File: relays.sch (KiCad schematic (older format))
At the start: 4 parts, among them U2 MCP23017-E_SP

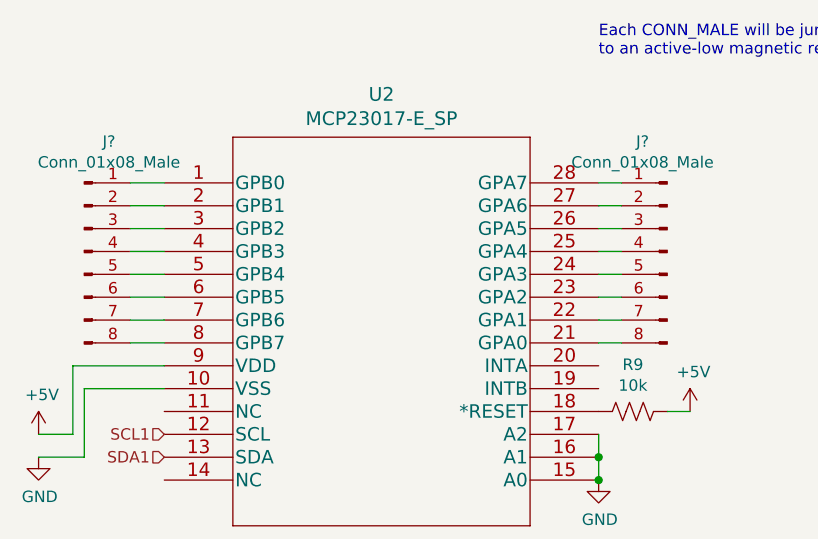
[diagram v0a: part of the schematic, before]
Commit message: Got rid of overlying duplicate parts
Some identical parts were placed over eachother which showed up when annotating references
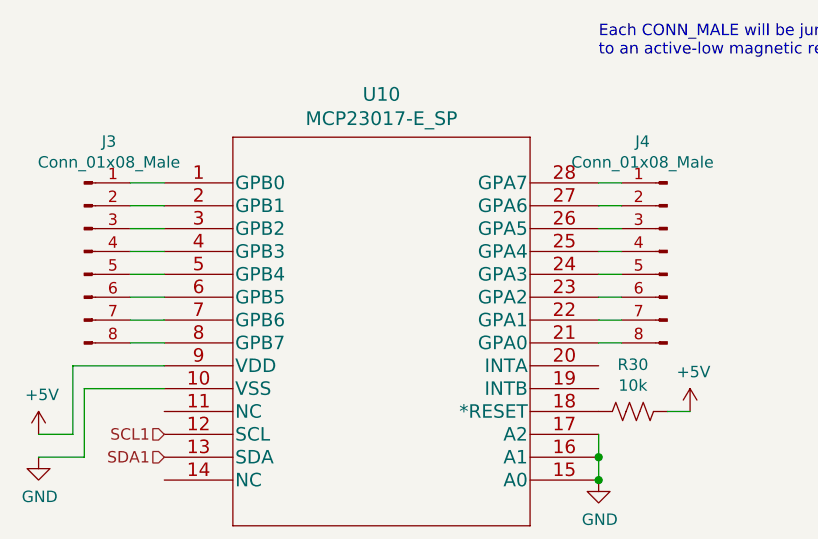
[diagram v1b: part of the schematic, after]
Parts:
- gave numbers to parts that had none: 2
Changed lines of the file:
@@
 SCL1
-$Comp
-L 2020-09-01_02-26-45:MCP23017-E_SP U2
-U 1 1 5F5A3B8E
-P 5000 2200
-AR Path="/5F57B52C/5F5A3B8E" Ref="U2"  Part="1"
-AR Path="/5F7C211E/5F5A3B8E" Ref="U?"  Part="1"
-F 0 "U?" H 5950 2587 60  0000 C CNN
-F 1 "MCP23017-E_SP" H 5950 2481 60  0000 C CNN
-F 2 "SPDIP28_300MC_MCH" H 5950 2440 60  0001 C CNN
-F 3 "" H 5000 2200 60  0000 C CNN
-	1    5000 2200
-	1    0    0    -1
-$EndComp
-Wire Wire Line
-	6900 3500 6900 3400
-Connection ~ 6900 3400
-Wire Wire Line
-	6900 3400 6900 3300
 $Comp
 L Device:R_US R9
@@
 P 7050 3200
 AR Path="/5F57B52C/5F5A3B84" Ref="R9"  Part="1"
-AR Path="/5F7C211E/5F5A3B84" Ref="R?"  Part="1"
-F 0 "R?" V 6845 3200 50  0000 C CNN
+AR Path="/5F7C211E/5F5A3B84" Ref="R30"  Part="1"
+F 0 "R30" V 6845 3200 50  0000 C CNN
 F 1 "10k" V 6936 3200 50  0000 C CNN
 F 2 "" V 7090 3190 50  0001 C CNN
@@
 $Comp
 L power:+5V #PWR0101
-U 1 1 5F5A3B7D
+U 1 1 5F733068
 P 7300 3200
-AR Path="/5F57B52C/5F5A3B7D" Ref="#PWR0101"  Part="1"
-AR Path="/5F7C211E/5F5A3B7D" Ref="#PWR?"  Part="1"
-F 0 "#PWR?" H 7300 3050 50  0001 C CNN
+AR Path="/5F57B52C/5F733068" Ref="#PWR0101"  Part="1"
+AR Path="/5F7C211E/5F733068" Ref="#PWR0153"  Part="1"
+F 0 "#PWR0153" H 7300 3050 50  0001 C CNN
 F 1 "+5V" H 7315 3373 50  0000 C CNN
 F 2 "" H 7300 3200 50  0001 C CNN
@@
 	1    0    0    -1
 $EndComp
-Connection ~ 6900 3500
 $Comp
 L power:GND #PWR0102
-U 1 1 5F5A3B69
+U 1 1 5F733065
 P 6900 3500
-AR Path="/5F57B52C/5F5A3B69" Ref="#PWR0102"  Part="1"
-AR Path="/5F7C211E/5F5A3B69" Ref="#PWR?"  Part="1"
-F 0 "#PWR?" H 6900 3250 50  0001 C CNN
+AR Path="/5F57B52C/5F733065" Ref="#PWR0102"  Part="1"
+AR Path="/5F7C211E/5F733065" Ref="#PWR0154"  Part="1"
+F 0 "#PWR0154" H 6900 3250 50  0001 C CNN
 F 1 "GND" H 6905 3327 50  0000 C CNN
 F 2 "" H 6900 3500 50  0001 C CNN
@@
 $Comp
 L power:GND #PWR0103
-U 1 1 5F5A3B6F
+U 1 1 5F733066
 P 4450 3400
-AR Path="/5F57B52C/5F5A3B6F" Ref="#PWR0103"  Part="1"
-AR Path="/5F7C211E/5F5A3B6F" Ref="#PWR?"  Part="1"
-F 0 "#PWR?" H 4450 3150 50  0001 C CNN
+AR Path="/5F57B52C/5F733066" Ref="#PWR0103"  Part="1"
+AR Path="/5F7C211E/5F733066" Ref="#PWR0155"  Part="1"
+F 0 "#PWR0155" H 4450 3150 50  0001 C CNN
 F 1 "GND" H 4455 3227 50  0000 C CNN
 F 2 "" H 4450 3400 50  0001 C CNN
@@
 $Comp
 L power:+5V #PWR0104
-U 1 1 5F5A3B75
+U 1 1 5F733067
 P 4450 3300
-AR Path="/5F57B52C/5F5A3B75" Ref="#PWR0104"  Part="1"
-AR Path="/5F7C211E/5F5A3B75" Ref="#PWR?"  Part="1"
-F 0 "#PWR?" H 4450 3150 50  0001 C CNN
+AR Path="/5F57B52C/5F733067" Ref="#PWR0104"  Part="1"
+AR Path="/5F7C211E/5F733067" Ref="#PWR0156"  Part="1"
+F 0 "#PWR0156" H 4450 3150 50  0001 C CNN
 F 1 "+5V" H 4465 3473 50  0000 C CNN
 F 2 "" H 4450 3300 50  0001 C CNN
@@
 	4650 3400 4450 3400
 $Comp
-L Connector:Conn_01x08_Male J?
+L Connector:Conn_01x08_Male J3
 U 1 1 5F7D661D
 P 4650 2500
-F 0 "J?" H 4758 2981 50  0000 C CNN
+F 0 "J3" H 4758 2981 50  0000 C CNN
 F 1 "Conn_01x08_Male" H 4758 2890 50  0000 C CNN
 F 2 "" H 4650 2500 50  0001 C CNN
@@
 $EndComp
 $Comp
-L Connector:Conn_01x08_Male J?
+L Connector:Conn_01x08_Male J4
 U 1 1 5F7DB213
 P 7200 2500
-F 0 "J?" H 7308 2981 50  0000 C CNN
+F 0 "J4" H 7308 2981 50  0000 C CNN
 F 1 "Conn_01x08_Male" H 7308 2890 50  0000 C CNN
 F 2 "" H 7200 2500 50  0001 C CNN
@@
 Text Notes 6900 1650 0    50   ~ 0
 Each CONN_MALE will be jumped\nto an active-low magnetic relay
+Wire Wire Line
+	6900 3400 6900 3300
+Wire Wire Line
+	6900 3500 6900 3400
+Connection ~ 6900 3400
+Connection ~ 6900 3500
+$Comp
+L 2020-09-01_02-26-45:MCP23017-E_SP U2
+U 1 1 5F73306A
+P 5000 2200
+AR Path="/5F57B52C/5F73306A" Ref="U2"  Part="1"
+AR Path="/5F7C211E/5F73306A" Ref="U10"  Part="1"
+F 0 "U10" H 5950 2587 60  0000 C CNN
+F 1 "MCP23017-E_SP" H 5950 2481 60  0000 C CNN
+F 2 "SPDIP28_300MC_MCH" H 5950 2440 60  0001 C CNN
+F 3 "" H 5000 2200 60  0000 C CNN
+	1    5000 2200
+	1    0    0    -1
+$EndComp
 $EndSCHEMATC

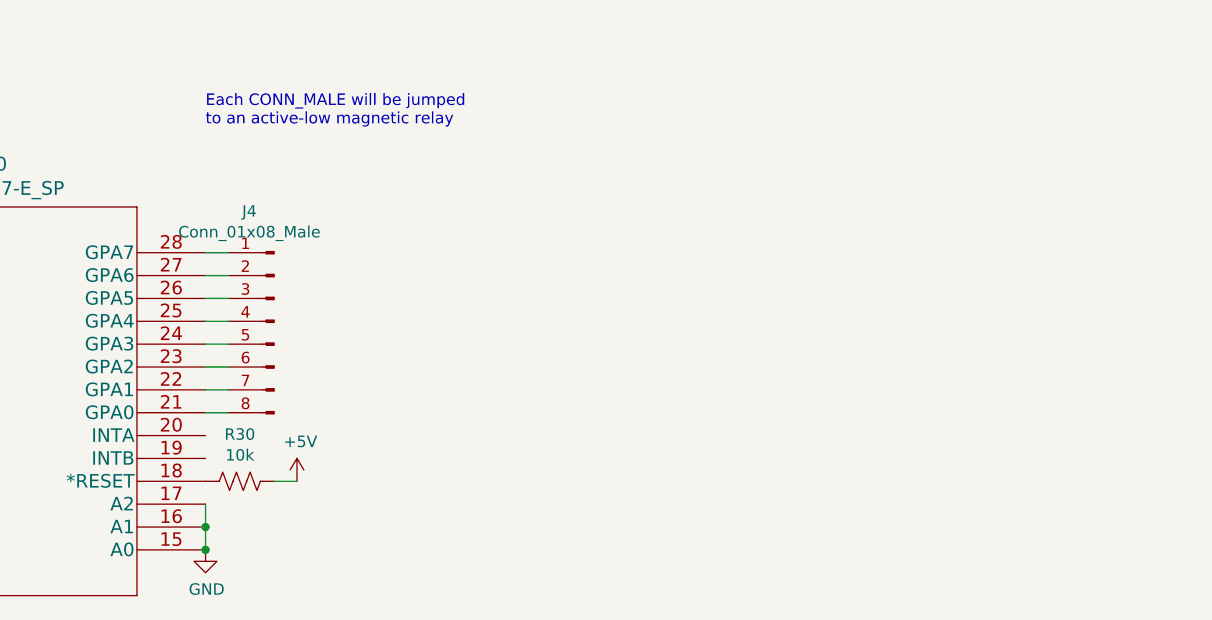
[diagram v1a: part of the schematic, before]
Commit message: Added Relays and diodes
Added relays and diodes per reviewer suggestion on the remote side connected to the MCP23017.
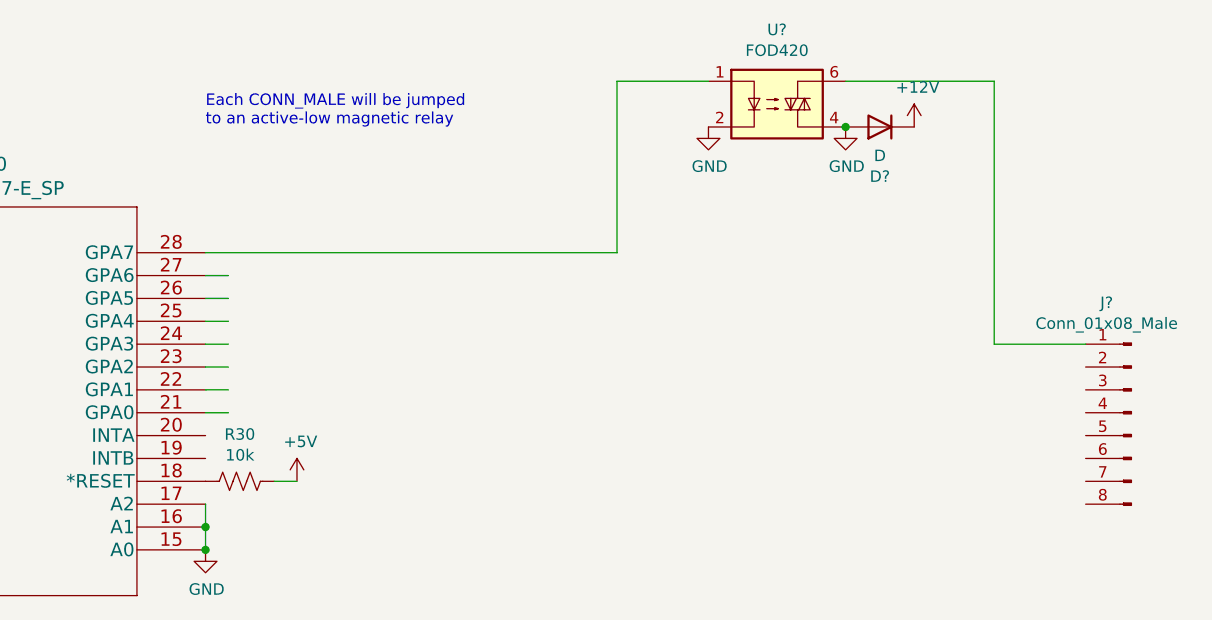
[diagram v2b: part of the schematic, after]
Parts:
- removed J4: Conn_01x08_Male, symbol Connector:Conn_01x08_Male
- added D?: D, symbol Device:D
- added J?: Conn_01x08_Male, symbol Connector:Conn_01x08_Male
- added U?: FOD420, Package_DIP:DIP-6_W7.62mm, symbol Relay_SolidState:FOD420
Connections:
- net labels added: +12V
- wire segments 25 -> 30
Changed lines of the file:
@@
 	1    0    0    -1
-$EndComp
-$Comp
-L Connector:Conn_01x08_Male J4
-U 1 1 5F7DB213
-P 7200 2500
-F 0 "J4" H 7308 2981 50  0000 C CNN
-F 1 "Conn_01x08_Male" H 7308 2890 50  0000 C CNN
-F 2 "" H 7200 2500 50  0001 C CNN
-F 3 "~" H 7200 2500 50  0001 C CNN
-	1    7200 2500
-	-1   0    0    -1
 $EndComp
 Wire Wire Line
@@
 	4850 2900 5000 2900
 Wire Wire Line
-	6900 2200 7000 2200
-Wire Wire Line
 	7000 2300 6900 2300
 Wire Wire Line
@@
 Wire Wire Line
 	7000 2900 6900 2900
-Text Notes 6900 1650 0    50   ~ 0
-Each CONN_MALE will be jumped\nto an active-low magnetic relay
 Wire Wire Line
 	6900 3400 6900 3300
@@
 	1    0    0    -1
 $EndComp
+Text Notes 6900 1650 0    50   ~ 0
+Each CONN_MALE will be jumped\nto an active-low magnetic relay
+$Comp
+L Relay_SolidState:FOD420 U?
+U 1 1 5F8B8DAE
+P 9400 1550
+F 0 "U?" H 9400 1875 50  0000 C CNN
+F 1 "FOD420" H 9400 1784 50  0000 C CNN
+F 2 "Package_DIP:DIP-6_W7.62mm" H 9200 1350 50  0001 L CIN
+F 3 "http://www.fairchildsemi.com/ds/FO/FOD4218.pdf" H 9400 1550 50  0001 L CNN
+	1    9400 1550
+	1    0    0    -1
+$EndComp
+Wire Wire Line
+	8700 2200 8700 1450
+Wire Wire Line
+	6900 2200 8700 2200
+$Comp
+L power:GND #PWR?
+U 1 1 5F8BC5BF
+P 9100 1650
+F 0 "#PWR?" H 9100 1400 50  0001 C CNN
+F 1 "GND" H 9105 1477 50  0000 C CNN
+F 2 "" H 9100 1650 50  0001 C CNN
+F 3 "" H 9100 1650 50  0001 C CNN
+	1    9100 1650
+	1    0    0    -1
+$EndComp
+Wire Wire Line
+	8700 1450 9100 1450
+$Comp
+L power:GND #PWR?
+U 1 1 5F8BDA28
+P 9700 1650
+F 0 "#PWR?" H 9700 1400 50  0001 C CNN
+F 1 "GND" H 9705 1477 50  0000 C CNN
+F 2 "" H 9700 1650 50  0001 C CNN
+F 3 "" H 9700 1650 50  0001 C CNN
+	1    9700 1650
+	1    0    0    -1
+$EndComp
+$Comp
+L Connector:Conn_01x08_Male J?
+U 1 1 5F8C1D14
+P 10950 2900
+F 0 "J?" H 11058 3381 50  0000 C CNN
+F 1 "Conn_01x08_Male" H 11058 3290 50  0000 C CNN
+F 2 "" H 10950 2900 50  0001 C CNN
+F 3 "~" H 10950 2900 50  0001 C CNN
+	1    10950 2900
+	-1   0    0    -1
+$EndComp
+Wire Wire Line
+	10350 1450 10350 2600
+Wire Wire Line
+	10350 2600 10750 2600
+$Comp
+L Device:D D?
+U 1 1 5F8C2E95
+P 9850 1650
+F 0 "D?" H 9850 1867 50  0000 C CNN
+F 1 "D" H 9850 1776 50  0000 C CNN
+F 2 "" H 9850 1650 50  0001 C CNN
+F 3 "~" H 9850 1650 50  0001 C CNN
+	1    9850 1650
+	-1   0    0    1
+$EndComp
+$Comp
+L power:+12V #PWR?
+U 1 1 5F8C4E97
+P 10000 1650
+F 0 "#PWR?" H 10000 1500 50  0001 C CNN
+F 1 "+12V" H 10015 1823 50  0000 C CNN
+F 2 "" H 10000 1650 50  0001 C CNN
+F 3 "" H 10000 1650 50  0001 C CNN
+	1    10000 1650
+	1    0    0    -1
+$EndComp
+Wire Wire Line
+	9700 1450 10350 1450
+Connection ~ 9700 1650
 $EndSCHEMATC

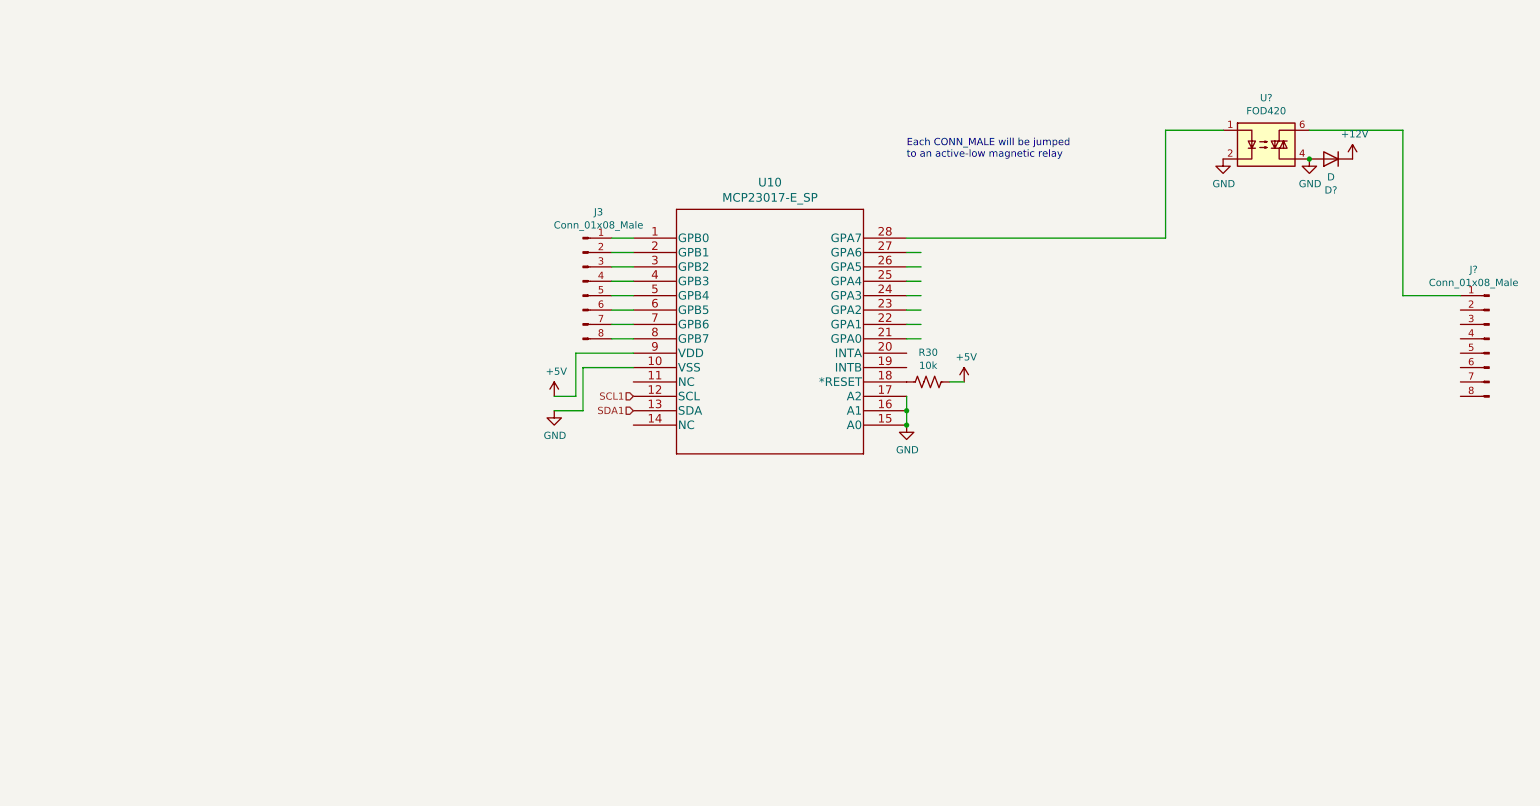
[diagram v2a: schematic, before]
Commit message: Added 5V connection on ethernet
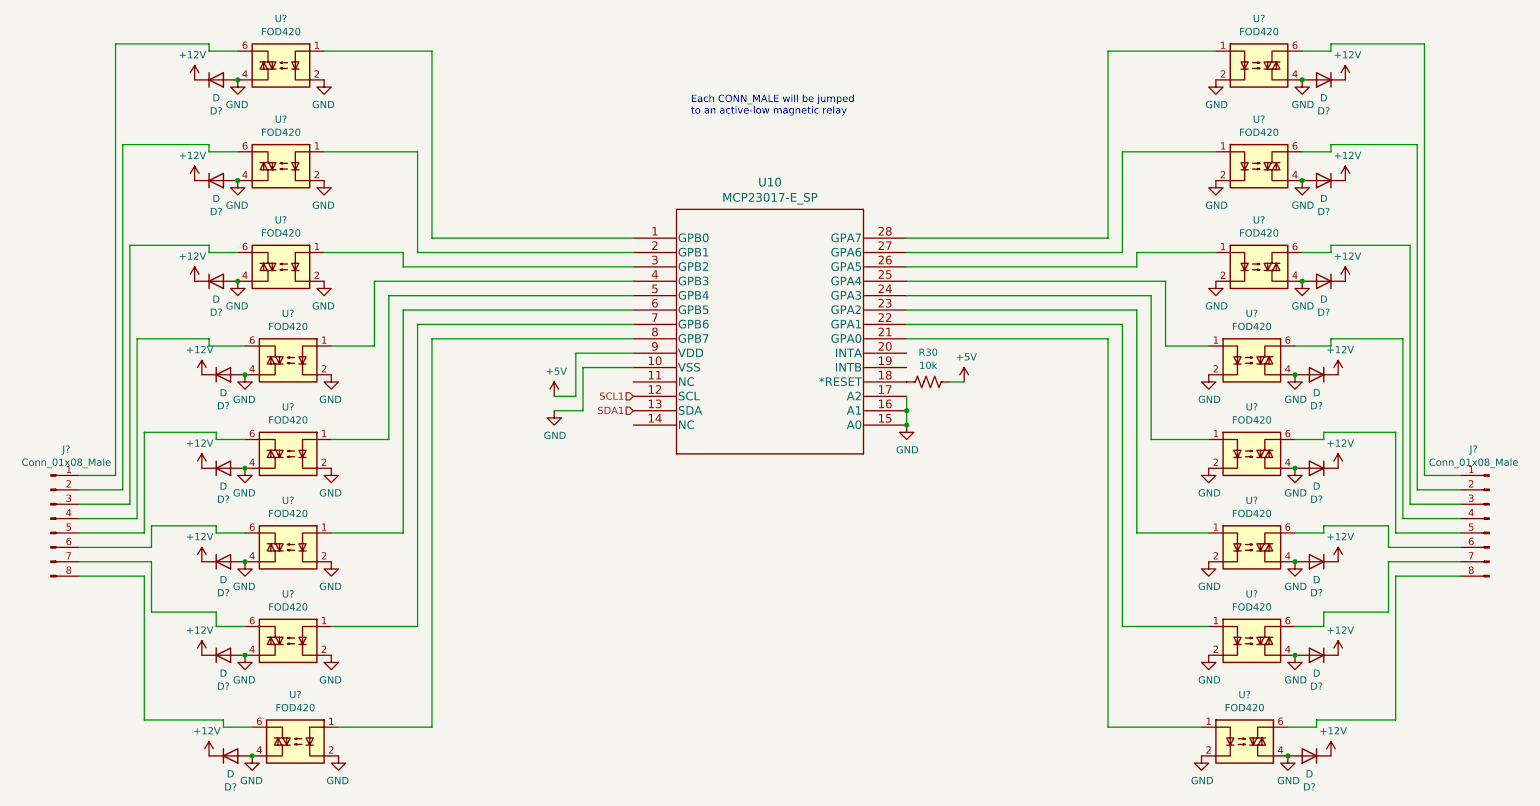
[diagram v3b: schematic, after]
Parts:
- removed J3: Conn_01x08_Male, symbol Connector:Conn_01x08_Male
- added D? (x15): D, symbol Device:D
- added J?: Conn_01x08_Male, symbol Connector:Conn_01x08_Male
- added U? (x15): FOD420, Package_DIP:DIP-6_W7.62mm, symbol Relay_SolidState:FOD420
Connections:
- wire segments 30 -> 137
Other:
- moved on the sheet: D?, J?, U?
